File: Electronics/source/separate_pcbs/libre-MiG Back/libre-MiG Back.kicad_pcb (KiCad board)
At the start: 2 copper layers, 18 x 28 mm, 4 parts, among them J17 Conn_01x06, SW18 SKRHABE010

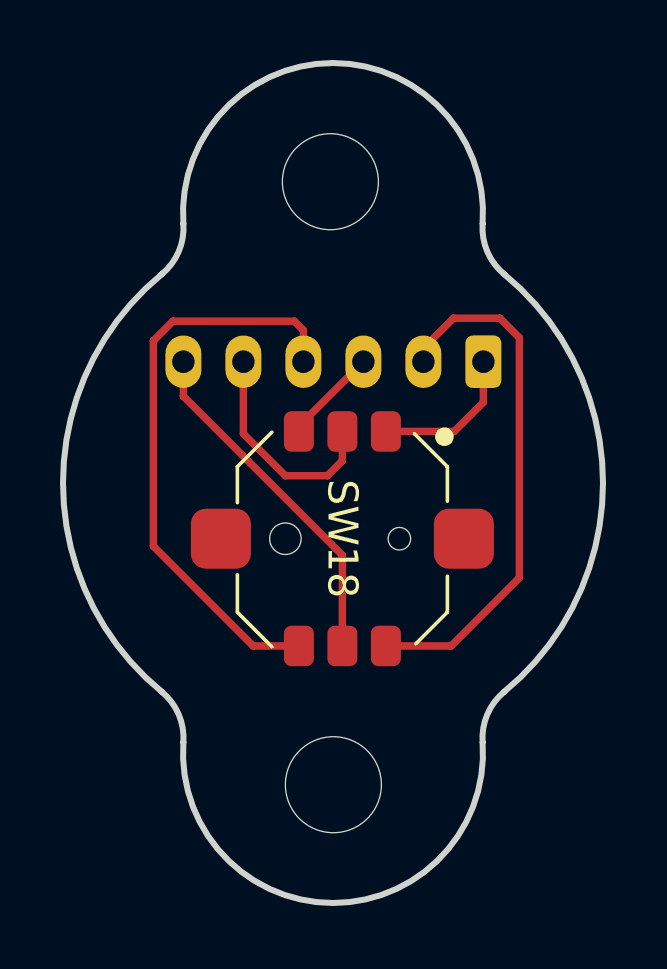
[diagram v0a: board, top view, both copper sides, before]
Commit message: added mechanical ignore
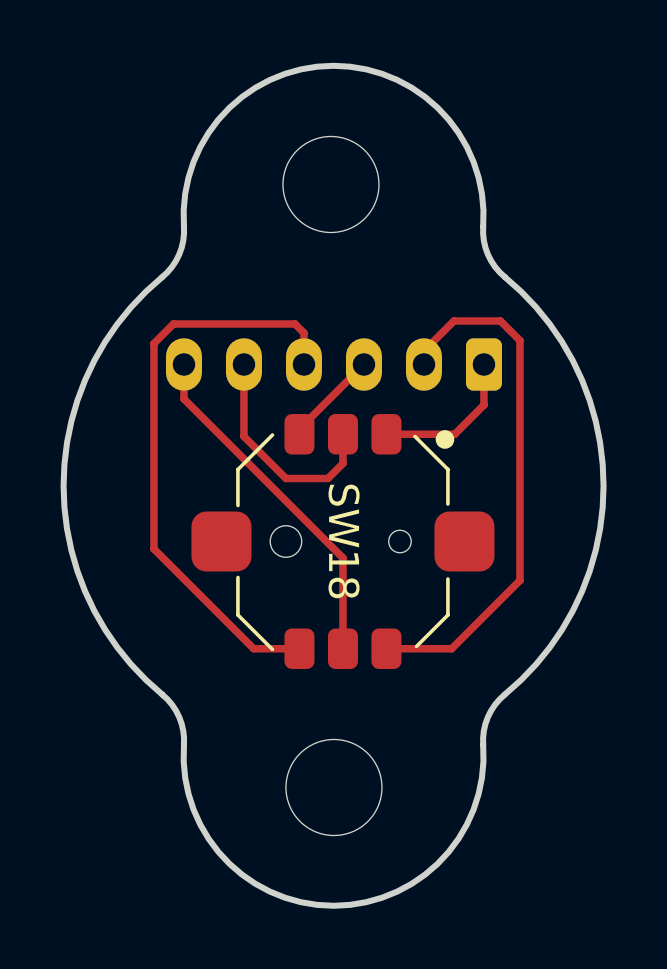
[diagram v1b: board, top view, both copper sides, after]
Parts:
- removed the REF** at (115.6, 185.9)
- removed the REF** at (115.5, 165.8)
- added REF**: MountingHole_3.2mm_M3, MountingHole:MountingHole_3.2mm_M3, F.Cu at (115.5, 165.9)
- added REF**: MountingHole_3.2mm_M3, MountingHole:MountingHole_3.2mm_M3, F.Cu at (115.6, 186.0)
- moved J17 0.09 mm to (120.6, 171.9)
- moved SW18 0.09 mm to (115.9, 177.8)
